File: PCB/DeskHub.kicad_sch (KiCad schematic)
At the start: 67 parts, among them J1 USB_A, J2 5V Barrel, U1 TUSB4041I, U2 3.3V Reg, U3 1.1V Reg, Y1 24MHz

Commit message: comply with ERC
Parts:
- U3: footprint TPS74801RGWR:QFN65P500X500X100-21N -> my_global:QFN65P500X500X100-21N; symbol MyLibrary:TPS74801RGWR -> my_global:TPS74801RGWR
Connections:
- net BOARD_3.3: no longer C44.1, C45.1, D2.2 (A), U2.3 (VO)
- net BOARD_3.3V: now also C44.1, C45.1, D2.2 (A), U2.3 (VO)
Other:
- moved on the sheet: C10, C13, C14, C15, C16, C17, C18, C19, C2, C20, C21, C23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

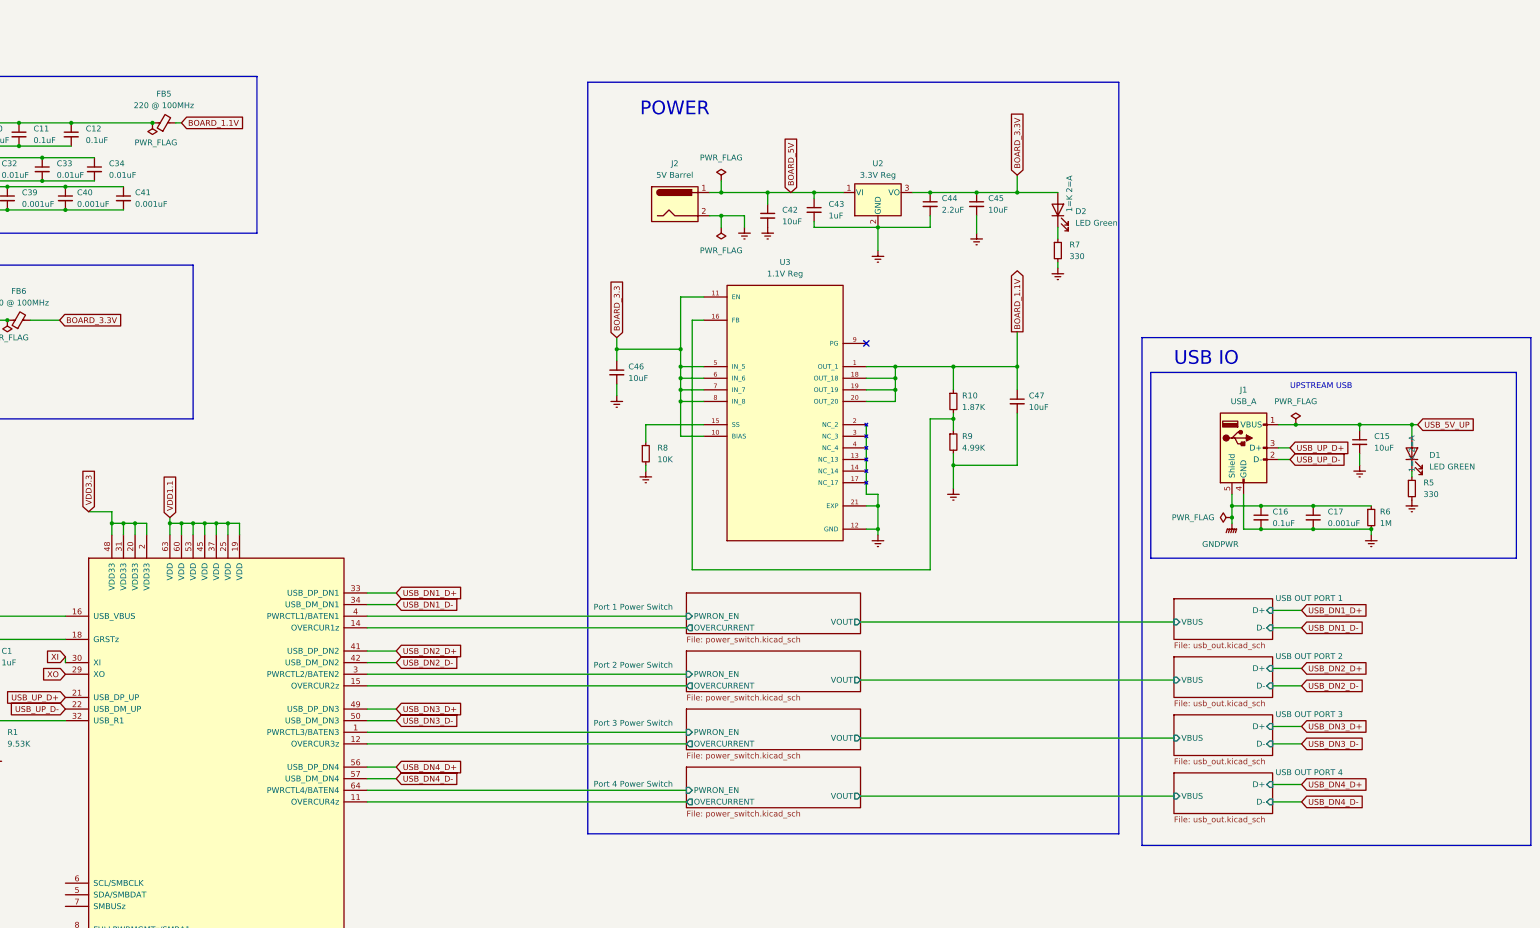
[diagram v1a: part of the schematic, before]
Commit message: add net classes
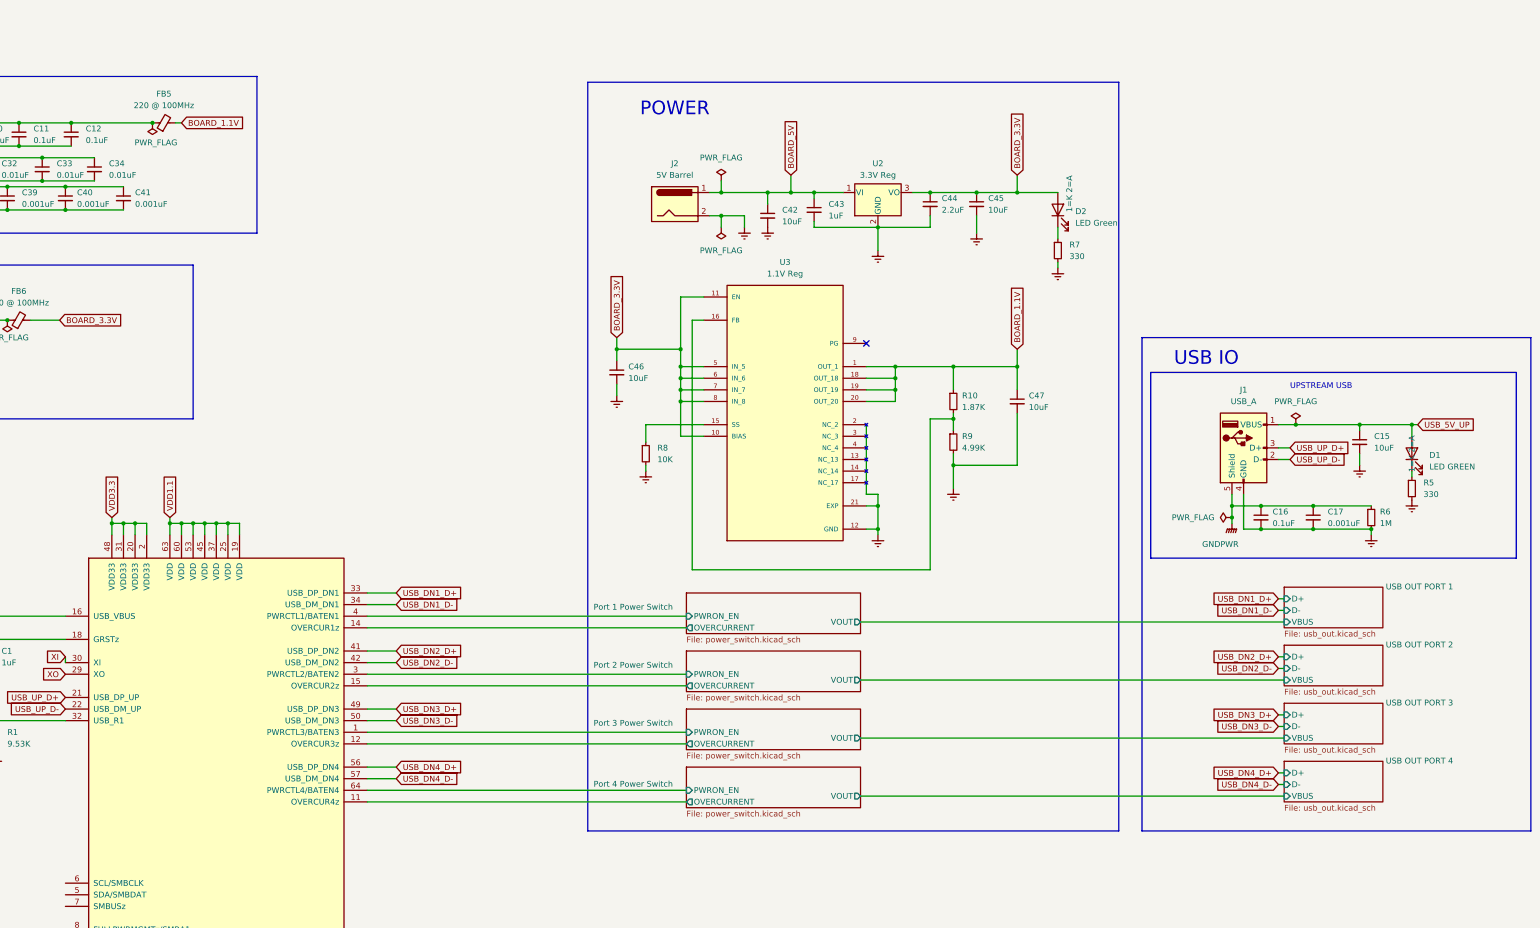
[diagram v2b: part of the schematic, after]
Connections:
- net BOARD_3.3 is gone; now on net BOARD_3.3V: C46.1, U3.10 (BIAS), U3.11 (EN), U3.5 (IN_5), U3.6 (IN_6), U3.7 (IN_7), U3.8 (IN_8)
